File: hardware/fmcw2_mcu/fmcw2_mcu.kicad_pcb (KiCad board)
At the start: 4 copper layers, 32.3 x 33.3 mm, 123 parts, among them CON1 BARREL_JACK, P1 CONN_15X2, P2 CONN_1, P3 CONN_1, P4 CONN_1, P5 CONN_1, P6 CONN_5, P7 CONN_6, Q1 RE1C002UN, Q2 RE1C002UN, SW1 DFU_PUSH, SW2 DFU_PUSH, U1 MAX1426, U16 USB-MICRO, U2 LT1817, U3 W25Q32FV, U4 LPC4320_BGA, U5 AOZ1281, U6 AOZ1281, U7 LP2985, U8 MCP4022-202, U9 FDC6329L, X1 12MHz

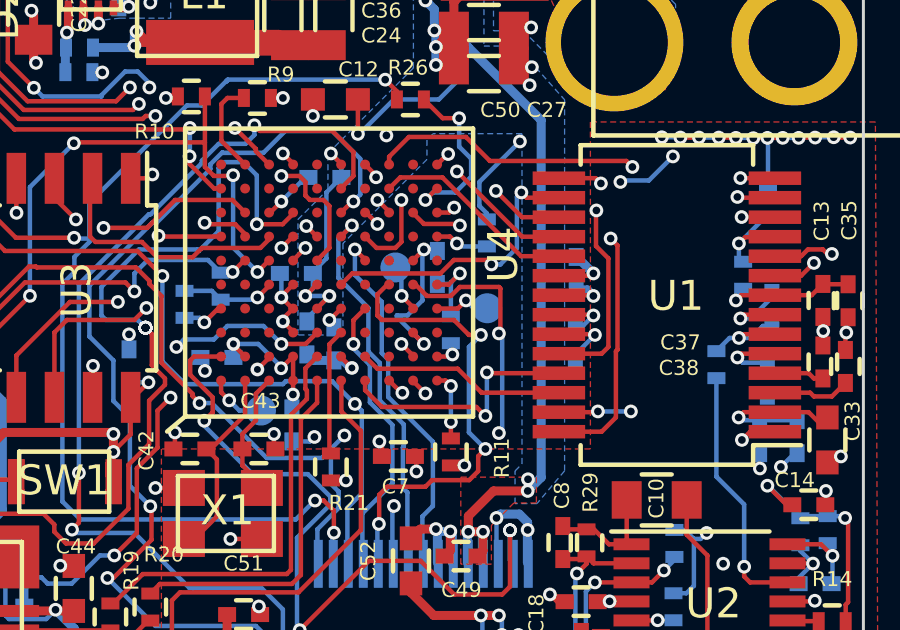
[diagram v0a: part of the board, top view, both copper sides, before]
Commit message: Add jump wire transistor
Scretches the ramp complete pulse from ADF4158.
Internal pull-up resistor of the microcontroller pin is used
to pull-up the transistor drain.
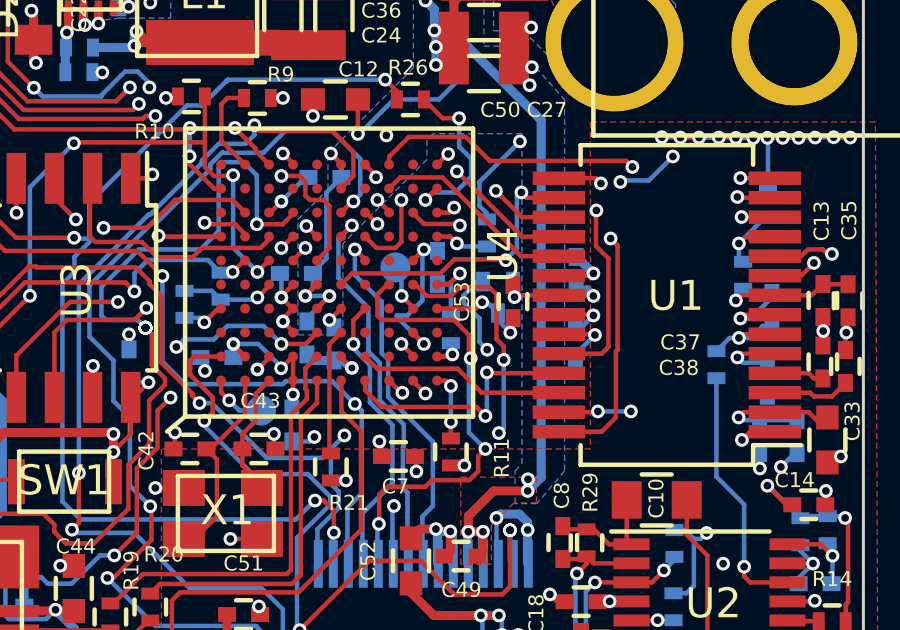
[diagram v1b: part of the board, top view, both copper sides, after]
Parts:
- removed P5: CONN_1, fmcw2:TP_1.00
- added C53: DNP, fmcw2:C_0402b, F.Cu at (138.4, 85.0)
- added Q3: RE1C002UN, fmcw2:SOT-416, B.Cu at (137.4, 84.3)
- C18, C8: value 10p -> 33p
- R28, R30: value 2.5k -> 2.49k
- R29: value 10k -> 1k
- R35: value 10k -> 4.7k
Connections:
- U4 pad K4: Net-(P5-Pad1) -> /~RAMP
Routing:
- net /SSP1_MISO: track 26.3 -> 34.8 mm, vias 3 -> 4
- net /~RAMP: track 0.00 -> 3.60 mm, vias 0 -> 2
- net GND: track 160.6 -> 163.1 mm, vias 99 -> 100
- net Net-(P5-Pad1): track 1.89 -> 0.00 mm, vias 1 -> 0
- net /ADF_LE: track 15.9 -> 15.4 mm
